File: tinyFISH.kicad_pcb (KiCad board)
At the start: 2 copper layers, 20 x 20 mm, 88 parts, among them Q1 SI2302DS, U1 CC2510, U2 MPU-6000, U3 LP2985AIM5-3.0/NOPB, U4 STM32F303CCTx, U5 M25P16-VME, U6 MICRO_USB_B, U7 INA139, X1 26MHz, X2 8MHz

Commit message: fixed rev id
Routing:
- net (no net): track 0.00 -> 2.50 mm
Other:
- board text added: "03/2017"
- board text added: "REV 0.2b"
- board text removed: "01/2017"
- board text removed: "REV 0.2"

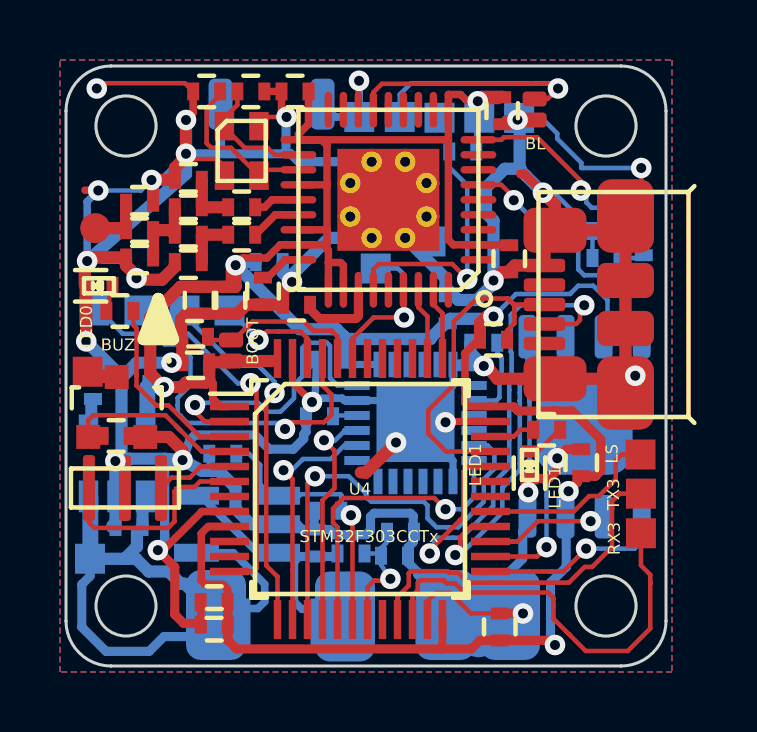
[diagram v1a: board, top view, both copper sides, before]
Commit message: fixed naming of pads
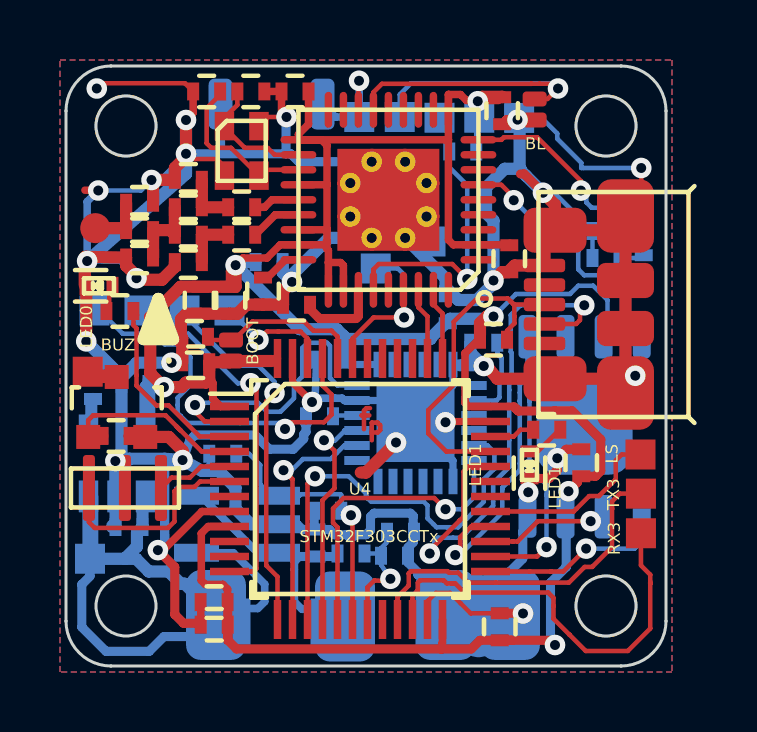
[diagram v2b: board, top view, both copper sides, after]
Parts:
- TP_ESC_2: renamed from TP_ESC_3; value ESC_3 -> ESC_2
- TP_ESC_3: renamed from TP_ESC_2; value ESC_2 -> ESC_3
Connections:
- TP_ESC_2 pad 1: ESC_3 -> ESC_2
- TP_ESC_3 pad 1: ESC_2 -> ESC_3
- U1 pad 1: Net-(U1-Pad1) -> (no net)
- U1 pad 11: Net-(U1-Pad11) -> (no net)
- U1 pad 12: Net-(U1-Pad12) -> (no net)
- U1 pad 13: Net-(U1-Pad13) -> (no net)
- U1 pad 14: Net-(U1-Pad14) -> (no net)
- U1 pad 17: Net-(U1-Pad17) -> (no net)
- U1 pad 18: Net-(U1-Pad18) -> (no net)
- U1 pad 3: Net-(U1-Pad3) -> (no net)
- U1 pad 32: Net-(U1-Pad32) -> (no net)
- U1 pad 36: Net-(U1-Pad36) -> (no net)
- U1 pad 4: Net-(U1-Pad4) -> (no net)
- U1 pad 5: Net-(U1-Pad5) -> (no net)
- U1 pad 7: Net-(U1-Pad7) -> (no net)
- U1 pad 8: Net-(U1-Pad8) -> (no net)
- U2 pad 14: Net-(U2-Pad14) -> (no net)
- U2 pad 15: Net-(U2-Pad15) -> (no net)
- U2 pad 16: Net-(U2-Pad16) -> (no net)
- U2 pad 17: Net-(U2-Pad17) -> (no net)
- U2 pad 19: Net-(U2-Pad19) -> (no net)
- U2 pad 2: Net-(U2-Pad2) -> (no net)
- U2 pad 21: Net-(U2-Pad21) -> (no net)
- U2 pad 22: Net-(U2-Pad22) -> (no net)
- U2 pad 3: Net-(U2-Pad3) -> (no net)
- U2 pad 4: Net-(U2-Pad4) -> (no net)
- U2 pad 5: Net-(U2-Pad5) -> (no net)
- U2 pad 6: Net-(U2-Pad6) -> (no net)
- U2 pad 7: Net-(U2-Pad7) -> (no net)
- U4 pad 10: Net-(U4-Pad10) -> (no net)
- U4 pad 11: Net-(U4-Pad11) -> (no net)
- U4 pad 12: ESC_2 -> ESC_3
- U4 pad 13: ESC_3 -> ESC_2
- U4 pad 20: Net-(U4-Pad20) -> (no net)
- U4 pad 30: Net-(U4-Pad30) -> (no net)
- U4 pad 31: Net-(U4-Pad31) -> (no net)
- U4 pad 39: Net-(U4-Pad39) -> (no net)
- U4 pad 40: Net-(U4-Pad40) -> (no net)
- U4 pad 41: Net-(U4-Pad41) -> (no net)
- U4 pad 42: Net-(U4-Pad42) -> (no net)
- U4 pad 7: Net-(U4-Pad7) -> (no net)
- U6 pad 1: Net-(U6-Pad1) -> (no net)
- U6 pad 4: Net-(U6-Pad4) -> (no net)
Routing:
- net (no net): track 2.50 -> 5.01 mm
- net ESC_3: track 12.8 -> 11.9 mm
- net ESC_2: track 11.9 -> 12.8 mm
